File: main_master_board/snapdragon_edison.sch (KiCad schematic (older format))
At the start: 54 parts, among them J2 JD2-0011NL, U17 J1, U18 J2, U19 LAN9512, U21 MIC2026, U23 antenna, U24 AS1360, U25 Si1900DL, U26 SN74LV4T125, U27 SN74LV4T125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

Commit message: Forgot to save before pushing last commit.
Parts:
- R26, R27, R29, R30, R32: footprint Resistors_SMD:R_0603 -> Resistors_SMD:R_0402
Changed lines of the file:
@@
 F 0 "R32" V 4480 7075 50  0000 C CNN
 F 1 "12.0K" V 4400 7075 50  0000 C CNN
-F 2 "Resistors_SMD:R_0603" V 4330 7075 50  0001 C CNN
+F 2 "Resistors_SMD:R_0402" V 4330 7075 50  0001 C CNN
 F 3 "" H 4400 7075 50  0000 C CNN
 	1    4400 7075
@@
 F 0 "R30" V 4430 8500 50  0000 C CNN
 F 1 "12.4K" V 4350 8500 50  0000 C CNN
-F 2 "Resistors_SMD:R_0603" V 4280 8500 50  0001 C CNN
+F 2 "Resistors_SMD:R_0402" V 4280 8500 50  0001 C CNN
 F 3 "" H 4350 8500 50  0000 C CNN
 	1    4350 8500
@@
 F 0 "R27" V 4180 8625 50  0000 C CNN
 F 1 "10.0K" V 4100 8625 50  0000 C CNN
-F 2 "Resistors_SMD:R_0603" V 4030 8625 50  0001 C CNN
+F 2 "Resistors_SMD:R_0402" V 4030 8625 50  0001 C CNN
 F 3 "" H 4100 8625 50  0000 C CNN
 	1    4100 8625
@@
 F 0 "R29" V 4280 9475 50  0000 C CNN
 F 1 "10.0K" V 4200 9475 50  0000 C CNN
-F 2 "Resistors_SMD:R_0603" V 4130 9475 50  0001 C CNN
+F 2 "Resistors_SMD:R_0402" V 4130 9475 50  0001 C CNN
 F 3 "" H 4200 9475 50  0000 C CNN
 	1    4200 9475
@@
 F 0 "R26" V 3955 6950 50  0000 C CNN
 F 1 "825" V 3875 6950 50  0000 C CNN
-F 2 "Resistors_SMD:R_0603" V 3805 6950 50  0001 C CNN
+F 2 "Resistors_SMD:R_0402" V 3805 6950 50  0001 C CNN
 F 3 "" H 3875 6950 50  0000 C CNN
 	1    3875 6950

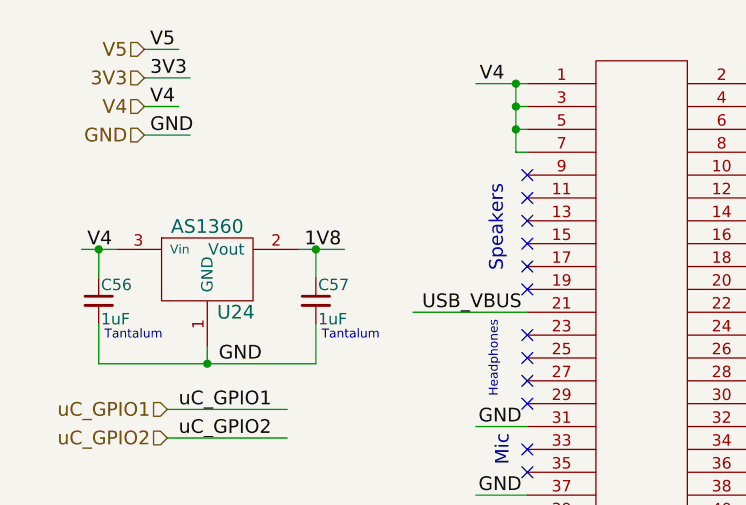
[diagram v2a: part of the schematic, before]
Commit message: Messed up and routed the lan9512 is a bad spot.
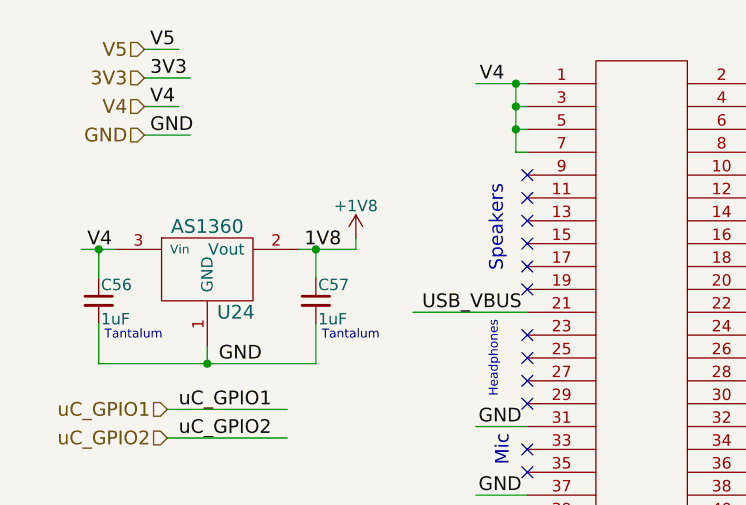
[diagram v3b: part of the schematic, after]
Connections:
- wire segments 401 -> 402
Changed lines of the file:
@@
 GND
 $Comp
-L +3.3VA #PWR025
+L +3.3VA #PWR027
 U 1 1 58837660
 P 3025 5775
-F 0 "#PWR025" H 3025 5625 50  0001 C CNN
+F 0 "#PWR027" H 3025 5625 50  0001 C CNN
 F 1 "+3.3VA" H 3025 5915 50  0000 C CNN
 F 2 "" H 3025 5775 50  0000 C CNN
@@
 GND
 $Comp
-L +1V8 #PWR026
+L +1V8 #PWR028
 U 1 1 5884251A
 P 875 7125
-F 0 "#PWR026" H 875 6975 50  0001 C CNN
+F 0 "#PWR028" H 875 6975 50  0001 C CNN
 F 1 "+1V8" H 875 7265 50  0000 C CNN
 F 2 "" H 875 7125 50  0000 C CNN
@@
 3V3
 $Comp
-L +3.3VA #PWR027
+L +3.3VA #PWR029
 U 1 1 5884804C
 P 7725 5500
-F 0 "#PWR027" H 7725 5350 50  0001 C CNN
+F 0 "#PWR029" H 7725 5350 50  0001 C CNN
 F 1 "+3.3VA" H 7725 5640 50  0000 C CNN
 F 2 "" H 7725 5500 50  0000 C CNN
@@
 $EndComp
 $Comp
-L +1V8 #PWR028
+L +1V8 #PWR030
 U 1 1 58849901
 P 4400 6225
-F 0 "#PWR028" H 4400 6075 50  0001 C CNN
+F 0 "#PWR030" H 4400 6075 50  0001 C CNN
 F 1 "+1V8" H 4400 6365 50  0000 C CNN
 F 2 "" H 4400 6225 50  0000 C CNN
@@
 $EndComp
 $Comp
-L +3.3VA #PWR029
+L +3.3VA #PWR031
 U 1 1 5885B0EB
 P 10325 8100
-F 0 "#PWR029" H 10325 7950 50  0001 C CNN
+F 0 "#PWR031" H 10325 7950 50  0001 C CNN
 F 1 "+3.3VA" H 10325 8240 50  0000 C CNN
 F 2 "" H 10325 8100 50  0000 C CNN
@@
 	800  1525 950  1525
 Wire Wire Line
-	1750 1525 1950 1525
+	1750 1525 2000 1525
 Wire Wire Line
 	875  1525 875  1650
@@
 Text Label 14675 4525 2    60   ~ 0
 USBD3_N
+$Comp
+L +1V8 #PWR?
+U 1 1 589E2381
+P 2000 1475
+F 0 "#PWR?" H 2000 1325 50  0001 C CNN
+F 1 "+1V8" H 2000 1615 50  0000 C CNN
+F 2 "" H 2000 1475 50  0000 C CNN
+F 3 "" H 2000 1475 50  0000 C CNN
+	1    2000 1475
+	1    0    0    -1
+$EndComp
+Wire Wire Line
+	2000 1525 2000 1475
 $EndSCHEMATC

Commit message: Working on routing all of the DART board
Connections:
- net labels added: GPIO106, GPIO112
- net labels removed: GPIO26, GPIO30, GPIO_30
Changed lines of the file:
@@
 Text Label 3775 5200 0    60   ~ 0
 GPIO_29
-Text Label 14700 6175 2    60   ~ 0
-GPIO_30
 Text Label 3775 4900 0    60   ~ 0
 GPIO_26
@@
 NoConn ~ 2750 2100
 NoConn ~ 2750 2200
-Text Label 2725 1800 2    60   ~ 0
-USB_VBUS
 NoConn ~ 2750 2400
 NoConn ~ 2750 2500
@@
 Wire Wire Line
 	2525 3000 2750 3000
-Wire Wire Line
-	2750 1800 2250 1800
 Connection ~ 2700 1000
 Wire Wire Line
@@
 GPIO27
 Text HLabel 14725 6075 2    60   Output ~ 0
-GPIO26
+GPIO106
 Text HLabel 14725 5975 2    60   Output ~ 0
 GPIO28
 Text HLabel 14725 6175 2    60   Output ~ 0
-GPIO30
+GPIO112
 Text Label 14700 4975 2    60   ~ 0
 GPIO_114
@@
 Wire Wire Line
 	14725 5275 14325 5275
-Text Label 14700 6075 2    60   ~ 0
-GPIO_26
 Text Label 14700 5975 2    60   ~ 0
 GPIO_28
@@
 USBD3_N
 $Comp
-L +1V8 #PWR?
+L +1V8 #PWR032
 U 1 1 589E2381
 P 2000 1475
-F 0 "#PWR?" H 2000 1325 50  0001 C CNN
+F 0 "#PWR032" H 2000 1325 50  0001 C CNN
 F 1 "+1V8" H 2000 1615 50  0000 C CNN
 F 2 "" H 2000 1475 50  0000 C CNN
@@
 Wire Wire Line
 	2000 1525 2000 1475
+Text Label 14700 6175 2    60   ~ 0
+GPIO_112
+Text Label 14700 6075 2    60   ~ 0
+GPIO_106
+Wire Wire Line
+	2750 1800 2250 1800
+Text Label 2725 1800 2    60   ~ 0
+USB_VBUS
 $EndSCHEMATC

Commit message: more routing. Started on PIC now.
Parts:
- added R65: 30, Resistors_SMD:R_0402, symbol R_Small
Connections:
- wire segments 402 -> 403
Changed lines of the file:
@@
 LIBS:Sensors
 LIBS:LP3852-3.3
-LIBS:decaWave
+LIBS:0s102011ma1qn1
+LIBS:74LVC1G17
+LIBS:74V1T126
+LIBS:acs711klctr-12ab-t
+LIBS:AD7192
+LIBS:AD7193
+LIBS:am-hrr30-xxx
+LIBS:aon7528
+LIBS:AP7363
+LIBS:AS1359
+LIBS:csd16323q3
+LIBS:dmn2004dmk
+LIBS:dp_devices
+LIBS:DSPIC33E128MC506
+LIBS:fds6898az
+LIBS:ina197
+LIBS:irf7329pbf
+LIBS:ld1117
+LIBS:lm3478
+LIBS:lm3481
+LIBS:lt1910
+LIBS:ltc1871
+LIBS:ltc1982
+LIBS:MAG3110
+LIBS:mcp1700
+LIBS:mcp73831
+LIBS:mcsmt-g5030a1-3712
+LIBS:microchip_can
+LIBS:microclasp_hdrx2
+LIBS:microclasp_hdrx3
+LIBS:MPU-6000_MPU-6050
+LIBS:MPU-9150
+LIBS:nrf24l01+
+LIBS:pds1040l
+LIBS:pic12f1571
+LIBS:pinhead
+LIBS:psmn013-80ys
+LIBS:RESISTOR_ARRAY
+LIBS:rf803d
+LIBS:RGB_LED
+LIBS:Si1970DH
+LIBS:sn65hvd232
+LIBS:ssc54
+LIBS:sw_push_4
+LIBS:tc74
+LIBS:TPS2113A
+LIBS:tps54540
+LIBS:vs-mbrb1635pbf
+LIBS:xal5050-562meb
+LIBS:xal6030-182mec
 LIBS:conn_2x50
 LIBS:conn_open_q_x2
@@
 LIBS:ac-dc
 LIBS:actel
-LIBS:allegro
 LIBS:Altera
 LIBS:analog_devices
@@
 LIBS:logo
 LIBS:maxim
-LIBS:mechanical
 LIBS:microchip_dspic33dsc
 LIBS:microchip_pic10mcu
@@
 LIBS:microchip_pic32mcu
 LIBS:motor_drivers
-LIBS:motors
 LIBS:msp430
 LIBS:nordicsemi
@@
 LIBS:ttl_ieee
 LIBS:video
-LIBS:wiznet
 LIBS:Worldsemi
 LIBS:Xicor
-LIBS:zetex
 LIBS:Zilog
 LIBS:conn_2x45
@@
 Text Label 3775 4400 0    60   ~ 0
 SPI1_CLK
-Text Label 3775 4500 0    60   ~ 0
+Text Label 4050 4500 0    60   ~ 0
 SPI1_MOSI
 Text Label 2725 4400 2    60   ~ 0
@@
 GND
 $Comp
-L +3.3VA #PWR027
+L +3.3VA #PWR29
 U 1 1 58837660
 P 3025 5775
-F 0 "#PWR027" H 3025 5625 50  0001 C CNN
+F 0 "#PWR29" H 3025 5625 50  0001 C CNN
 F 1 "+3.3VA" H 3025 5915 50  0000 C CNN
 F 2 "" H 3025 5775 50  0000 C CNN
@@
 GND
 $Comp
-L +1V8 #PWR028
+L +1V8 #PWR27
 U 1 1 5884251A
 P 875 7125
-F 0 "#PWR028" H 875 6975 50  0001 C CNN
+F 0 "#PWR27" H 875 6975 50  0001 C CNN
 F 1 "+1V8" H 875 7265 50  0000 C CNN
 F 2 "" H 875 7125 50  0000 C CNN
@@
 3V3
 $Comp
-L +3.3VA #PWR029
+L +3.3VA #PWR31
 U 1 1 5884804C
 P 7725 5500
-F 0 "#PWR029" H 7725 5350 50  0001 C CNN
+F 0 "#PWR31" H 7725 5350 50  0001 C CNN
 F 1 "+3.3VA" H 7725 5640 50  0000 C CNN
 F 2 "" H 7725 5500 50  0000 C CNN
@@
 $EndComp
 $Comp
-L +1V8 #PWR030
+L +1V8 #PWR30
 U 1 1 58849901
 P 4400 6225
-F 0 "#PWR030" H 4400 6075 50  0001 C CNN
+F 0 "#PWR30" H 4400 6075 50  0001 C CNN
 F 1 "+1V8" H 4400 6365 50  0000 C CNN
 F 2 "" H 4400 6225 50  0000 C CNN
@@
 $EndComp
 $Comp
-L +3.3VA #PWR031
+L +3.3VA #PWR32
 U 1 1 5885B0EB
 P 10325 8100
-F 0 "#PWR031" H 10325 7950 50  0001 C CNN
+F 0 "#PWR32" H 10325 7950 50  0001 C CNN
 F 1 "+3.3VA" H 10325 8240 50  0000 C CNN
 F 2 "" H 10325 8100 50  0000 C CNN
@@
 Text HLabel 14700 1750 2    60   Output ~ 0
 uC_CLK
-Text Label 8500 1125 2    60   ~ 0
+Text Label 8600 1225 2    60   ~ 0
 SPI1_CS_N
 Text Label 9850 2900 0    60   ~ 0
 SPI1_MISO_3V3
-Text Label 8500 1225 2    60   ~ 0
+Text Label 8600 1125 2    60   ~ 0
 SPI1_CLK
-Text Label 8500 1025 2    60   ~ 0
+Text Label 8600 1025 2    60   ~ 0
 SPI1_MOSI
 Text HLabel 14700 900  2    60   BiDi ~ 0
@@
 Text Label 9850 1025 0    60   ~ 0
 SPI1_MOSI_3V3
+Text Label 9850 1225 0    60   ~ 0
+SPI1_CS_N_3V3
 Text Label 9850 1125 0    60   ~ 0
-SPI1_CS_N_3V3
-Text Label 9850 1225 0    60   ~ 0
 SPI1_CLK_3V3
 Text Label 9850 1325 0    60   ~ 0
@@
 	2700 1100 2750 1100
 Wire Wire Line
-	3750 4500 4250 4500
+	4025 4500 4525 4500
 Wire Wire Line
 	3750 4400 4200 4400
@@
 USBD3_N
 $Comp
-L +1V8 #PWR032
+L +1V8 #PWR28
 U 1 1 589E2381
 P 2000 1475
-F 0 "#PWR032" H 2000 1325 50  0001 C CNN
+F 0 "#PWR28" H 2000 1325 50  0001 C CNN
 F 1 "+1V8" H 2000 1615 50  0000 C CNN
 F 2 "" H 2000 1475 50  0000 C CNN
@@
 Text Label 2725 1800 2    60   ~ 0
 USB_VBUS
+$Comp
+L R_Small R65
+U 1 1 58A31C89
+P 3925 4500
+F 0 "R65" V 3975 4600 50  0000 L CNN
+F 1 "30" V 3920 4450 50  0000 L CNN
+F 2 "Resistors_SMD:R_0402" H 3925 4500 50  0001 C CNN
+F 3 "" H 3925 4500 50  0000 C CNN
+	1    3925 4500
+	0    -1   -1   0
+$EndComp
+Wire Wire Line
+	3750 4500 3825 4500
 $EndSCHEMATC

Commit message: Routing the RGB leds. Also finished the dwm and nrf24L01
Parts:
- C34, C35, C36, C37, C38, C39, C40, C41, C42, C43, C44, C45, C46, C48, C49, C50: footprint Capacitors_SMD:C_0201 -> Capacitors_SMD:C_0402
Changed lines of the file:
@@
 LIBS:Sensors
 LIBS:LP3852-3.3
-LIBS:0s102011ma1qn1
-LIBS:74LVC1G17
-LIBS:74V1T126
-LIBS:acs711klctr-12ab-t
-LIBS:AD7192
-LIBS:AD7193
-LIBS:am-hrr30-xxx
-LIBS:aon7528
-LIBS:AP7363
-LIBS:AS1359
-LIBS:csd16323q3
-LIBS:dmn2004dmk
-LIBS:dp_devices
-LIBS:DSPIC33E128MC506
-LIBS:fds6898az
-LIBS:ina197
-LIBS:irf7329pbf
-LIBS:ld1117
-LIBS:lm3478
-LIBS:lm3481
-LIBS:lt1910
-LIBS:ltc1871
-LIBS:ltc1982
-LIBS:MAG3110
-LIBS:mcp1700
-LIBS:mcp73831
-LIBS:mcsmt-g5030a1-3712
-LIBS:microchip_can
-LIBS:microclasp_hdrx2
-LIBS:microclasp_hdrx3
-LIBS:MPU-6000_MPU-6050
-LIBS:MPU-9150
-LIBS:nrf24l01+
-LIBS:pds1040l
-LIBS:pic12f1571
-LIBS:pinhead
-LIBS:psmn013-80ys
-LIBS:RESISTOR_ARRAY
-LIBS:rf803d
-LIBS:RGB_LED
-LIBS:Si1970DH
-LIBS:sn65hvd232
-LIBS:ssc54
-LIBS:sw_push_4
-LIBS:tc74
-LIBS:TPS2113A
-LIBS:tps54540
-LIBS:vs-mbrb1635pbf
-LIBS:xal5050-562meb
-LIBS:xal6030-182mec
+LIBS:decaWave
 LIBS:conn_2x50
 LIBS:conn_open_q_x2
@@
 LIBS:ac-dc
 LIBS:actel
+LIBS:allegro
 LIBS:Altera
 LIBS:analog_devices
@@
 LIBS:logo
 LIBS:maxim
+LIBS:mechanical
 LIBS:microchip_dspic33dsc
 LIBS:microchip_pic10mcu
@@
 LIBS:microchip_pic32mcu
 LIBS:motor_drivers
+LIBS:motors
 LIBS:msp430
 LIBS:nordicsemi
@@
 LIBS:ttl_ieee
 LIBS:video
+LIBS:wiznet
 LIBS:Worldsemi
 LIBS:Xicor
+LIBS:zetex
 LIBS:Zilog
 LIBS:conn_2x45
@@
 F 0 "C35" H 1360 6070 50  0000 L CNN
 F 1 "0.1uF" V 1250 5900 50  0000 L CNN
-F 2 "Capacitors_SMD:C_0201" H 1350 6000 50  0001 C CNN
+F 2 "Capacitors_SMD:C_0402" H 1350 6000 50  0001 C CNN
 F 3 "" H 1350 6000 50  0000 C CNN
 F 4 "10V" V 1450 5950 60  0000 C CNN "Voltage"
@@
 F 0 "C38" H 1660 6070 50  0000 L CNN
 F 1 "0.1uF" V 1550 5900 50  0000 L CNN
-F 2 "Capacitors_SMD:C_0201" H 1650 6000 50  0001 C CNN
+F 2 "Capacitors_SMD:C_0402" H 1650 6000 50  0001 C CNN
 F 3 "" H 1650 6000 50  0000 C CNN
 F 4 "10V" V 1750 5950 60  0000 C CNN "Voltage"
@@
 F 0 "C41" H 1935 6070 50  0000 L CNN
 F 1 "0.1uF" V 1825 5900 50  0000 L CNN
-F 2 "Capacitors_SMD:C_0201" H 1925 6000 50  0001 C CNN
+F 2 "Capacitors_SMD:C_0402" H 1925 6000 50  0001 C CNN
 F 3 "" H 1925 6000 50  0000 C CNN
 F 4 "10V" V 2025 5950 60  0000 C CNN "Voltage"
@@
 F 0 "C43" H 2210 6070 50  0000 L CNN
 F 1 "0.1uF" V 2100 5900 50  0000 L CNN
-F 2 "Capacitors_SMD:C_0201" H 2200 6000 50  0001 C CNN
+F 2 "Capacitors_SMD:C_0402" H 2200 6000 50  0001 C CNN
 F 3 "" H 2200 6000 50  0000 C CNN
 F 4 "10V" V 2300 5950 60  0000 C CNN "Voltage"
@@
 F 0 "C45" H 2485 6070 50  0000 L CNN
 F 1 "0.1uF" V 2375 5900 50  0000 L CNN
-F 2 "Capacitors_SMD:C_0201" H 2475 6000 50  0001 C CNN
+F 2 "Capacitors_SMD:C_0402" H 2475 6000 50  0001 C CNN
 F 3 "" H 2475 6000 50  0000 C CNN
 F 4 "10V" V 2575 5950 60  0000 C CNN "Voltage"
@@
 F 0 "C48" H 2760 6070 50  0000 L CNN
 F 1 "0.1uF" V 2650 5900 50  0000 L CNN
-F 2 "Capacitors_SMD:C_0201" H 2750 6000 50  0001 C CNN
+F 2 "Capacitors_SMD:C_0402" H 2750 6000 50  0001 C CNN
 F 3 "" H 2750 6000 50  0000 C CNN
 F 4 "10V" V 2850 5950 60  0000 C CNN "Voltage"
@@
 F 0 "C50" H 3035 6070 50  0000 L CNN
 F 1 "0.1uF" V 2925 5900 50  0000 L CNN
-F 2 "Capacitors_SMD:C_0201" H 3025 6000 50  0001 C CNN
+F 2 "Capacitors_SMD:C_0402" H 3025 6000 50  0001 C CNN
 F 3 "" H 3025 6000 50  0000 C CNN
 F 4 "10V" V 3125 5950 60  0000 C CNN "Voltage"
@@
 GND
 $Comp
-L +3.3VA #PWR29
+L +3.3VA #PWR027
 U 1 1 58837660
 P 3025 5775
-F 0 "#PWR29" H 3025 5625 50  0001 C CNN
+F 0 "#PWR027" H 3025 5625 50  0001 C CNN
 F 1 "+3.3VA" H 3025 5915 50  0000 C CNN
 F 2 "" H 3025 5775 50  0000 C CNN
@@
 F 0 "C36" H 1360 6695 50  0000 L CNN
 F 1 "0.1uF" V 1250 6525 50  0000 L CNN
-F 2 "Capacitors_SMD:C_0201" H 1350 6625 50  0001 C CNN
+F 2 "Capacitors_SMD:C_0402" H 1350 6625 50  0001 C CNN
 F 3 "" H 1350 6625 50  0000 C CNN
 F 4 "10V" V 1450 6575 60  0000 C CNN "Voltage"
@@
 F 0 "C39" H 1660 6695 50  0000 L CNN
 F 1 "0.1uF" V 1550 6525 50  0000 L CNN
-F 2 "Capacitors_SMD:C_0201" H 1650 6625 50  0001 C CNN
+F 2 "Capacitors_SMD:C_0402" H 1650 6625 50  0001 C CNN
 F 3 "" H 1650 6625 50  0000 C CNN
 F 4 "10V" V 1750 6575 60  0000 C CNN "Voltage"
@@
 F 0 "C42" H 1935 6695 50  0000 L CNN
 F 1 "0.1uF" V 1825 6525 50  0000 L CNN
-F 2 "Capacitors_SMD:C_0201" H 1925 6625 50  0001 C CNN
+F 2 "Capacitors_SMD:C_0402" H 1925 6625 50  0001 C CNN
 F 3 "" H 1925 6625 50  0000 C CNN
 F 4 "10V" V 2025 6575 60  0000 C CNN "Voltage"
@@
 F 0 "C44" H 2210 6695 50  0000 L CNN
 F 1 "0.1uF" V 2100 6525 50  0000 L CNN
-F 2 "Capacitors_SMD:C_0201" H 2200 6625 50  0001 C CNN
+F 2 "Capacitors_SMD:C_0402" H 2200 6625 50  0001 C CNN
 F 3 "" H 2200 6625 50  0000 C CNN
 F 4 "10V" V 2300 6575 60  0000 C CNN "Voltage"
@@
 F 0 "C46" H 2485 6695 50  0000 L CNN
 F 1 "0.1uF" V 2375 6525 50  0000 L CNN
-F 2 "Capacitors_SMD:C_0201" H 2475 6625 50  0001 C CNN
+F 2 "Capacitors_SMD:C_0402" H 2475 6625 50  0001 C CNN
 F 3 "" H 2475 6625 50  0000 C CNN
 F 4 "10V" V 2575 6575 60  0000 C CNN "Voltage"
@@
 GND
 $Comp
-L +1V8 #PWR27
+L +1V8 #PWR028
 U 1 1 5884251A
 P 875 7125
-F 0 "#PWR27" H 875 6975 50  0001 C CNN
+F 0 "#PWR028" H 875 6975 50  0001 C CNN
 F 1 "+1V8" H 875 7265 50  0000 C CNN
 F 2 "" H 875 7125 50  0000 C CNN
@@
 F 0 "C34" H 1160 7420 50  0000 L CNN
 F 1 "0.1uF" V 1050 7250 50  0000 L CNN
-F 2 "Capacitors_SMD:C_0201" H 1150 7350 50  0001 C CNN
+F 2 "Capacitors_SMD:C_0402" H 1150 7350 50  0001 C CNN
 F 3 "" H 1150 7350 50  0000 C CNN
 F 4 "10V" V 1250 7300 60  0000 C CNN "Voltage"
@@
 F 0 "C37" H 1435 7420 50  0000 L CNN
 F 1 "0.1uF" V 1325 7250 50  0000 L CNN
-F 2 "Capacitors_SMD:C_0201" H 1425 7350 50  0001 C CNN
+F 2 "Capacitors_SMD:C_0402" H 1425 7350 50  0001 C CNN
 F 3 "" H 1425 7350 50  0000 C CNN
 F 4 "10V" V 1525 7300 60  0000 C CNN "Voltage"
@@
 F 0 "C49" H 3010 7445 50  0000 L CNN
 F 1 "0.1uF" V 2900 7275 50  0000 L CNN
-F 2 "Capacitors_SMD:C_0201" H 3000 7375 50  0001 C CNN
+F 2 "Capacitors_SMD:C_0402" H 3000 7375 50  0001 C CNN
 F 3 "" H 3000 7375 50  0000 C CNN
 F 4 "10V" V 3100 7325 60  0000 C CNN "Voltage"
@@
 F 0 "C40" H 1835 7445 50  0000 L CNN
 F 1 "1.0uF" V 1725 7275 50  0000 L CNN
-F 2 "Capacitors_SMD:C_0201" H 1825 7375 50  0001 C CNN
+F 2 "Capacitors_SMD:C_0402" H 1825 7375 50  0001 C CNN
 F 3 "" H 1825 7375 50  0000 C CNN
 F 4 "10V" V 1925 7325 60  0000 C CNN "Voltage"
@@
 3V3
 $Comp
-L +3.3VA #PWR31
+L +3.3VA #PWR029
 U 1 1 5884804C
 P 7725 5500
-F 0 "#PWR31" H 7725 5350 50  0001 C CNN
+F 0 "#PWR029" H 7725 5350 50  0001 C CNN
 F 1 "+3.3VA" H 7725 5640 50  0000 C CNN
 F 2 "" H 7725 5500 50  0000 C CNN
@@
 $EndComp
 $Comp
-L +1V8 #PWR30
+L +1V8 #PWR030
 U 1 1 58849901
 P 4400 6225
-F 0 "#PWR30" H 4400 6075 50  0001 C CNN
+F 0 "#PWR030" H 4400 6075 50  0001 C CNN
 F 1 "+1V8" H 4400 6365 50  0000 C CNN
 F 2 "" H 4400 6225 50  0000 C CNN
@@
 $EndComp
 $Comp
-L +3.3VA #PWR32
+L +3.3VA #PWR031
 U 1 1 5885B0EB
 P 10325 8100
-F 0 "#PWR32" H 10325 7950 50  0001 C CNN
+F 0 "#PWR031" H 10325 7950 50  0001 C CNN
 F 1 "+3.3VA" H 10325 8240 50  0000 C CNN
 F 2 "" H 10325 8100 50  0000 C CNN
@@
 USBD3_N
 $Comp
-L +1V8 #PWR28
+L +1V8 #PWR032
 U 1 1 589E2381
 P 2000 1475
-F 0 "#PWR28" H 2000 1325 50  0001 C CNN
+F 0 "#PWR032" H 2000 1325 50  0001 C CNN
 F 1 "+1V8" H 2000 1615 50  0000 C CNN
 F 2 "" H 2000 1475 50  0000 C CNN

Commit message: Finished Routing!!! DRC issues, but not sure if that is really an issue...
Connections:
- net labels added: GPIO12, GPIO13
- net labels removed: GPIO49, GPIO52
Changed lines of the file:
@@
 Text Label 5175 2100 2    60   ~ 0
 UART0_RX
-Text Label 5175 2200 2    60   ~ 0
+Text Label 5200 2200 2    60   ~ 0
 UART0_CTS_N
 Text Label 2725 3900 2    60   ~ 0
@@
 	2750 3200 2125 3200
 Wire Wire Line
-	5175 2200 4575 2200
+	5200 2200 4600 2200
 Wire Wire Line
 	5200 2100 4725 2100
@@
 GPIO113
 Text HLabel 14725 5275 2    60   Output ~ 0
-GPIO52
+GPIO13
 Text HLabel 14725 5375 2    60   Output ~ 0
-GPIO49
+GPIO12
 Text HLabel 14725 5575 2    60   Output ~ 0
 GPIO51
@@
 	14725 5175 14275 5175
 Text Label 14700 5275 2    60   ~ 0
-GPIO_52
+GPIO_13
 Text Label 14700 5375 2    60   ~ 0
-GPIO_49
+GPIO_12
 Text Label 14700 5475 2    60   ~ 0
 GPIO_50
